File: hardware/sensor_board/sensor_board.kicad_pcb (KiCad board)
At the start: 2 copper layers, 18 x 15 mm, 4 parts, among them J0 Conn_01x04, U0 HIHxx3x-021

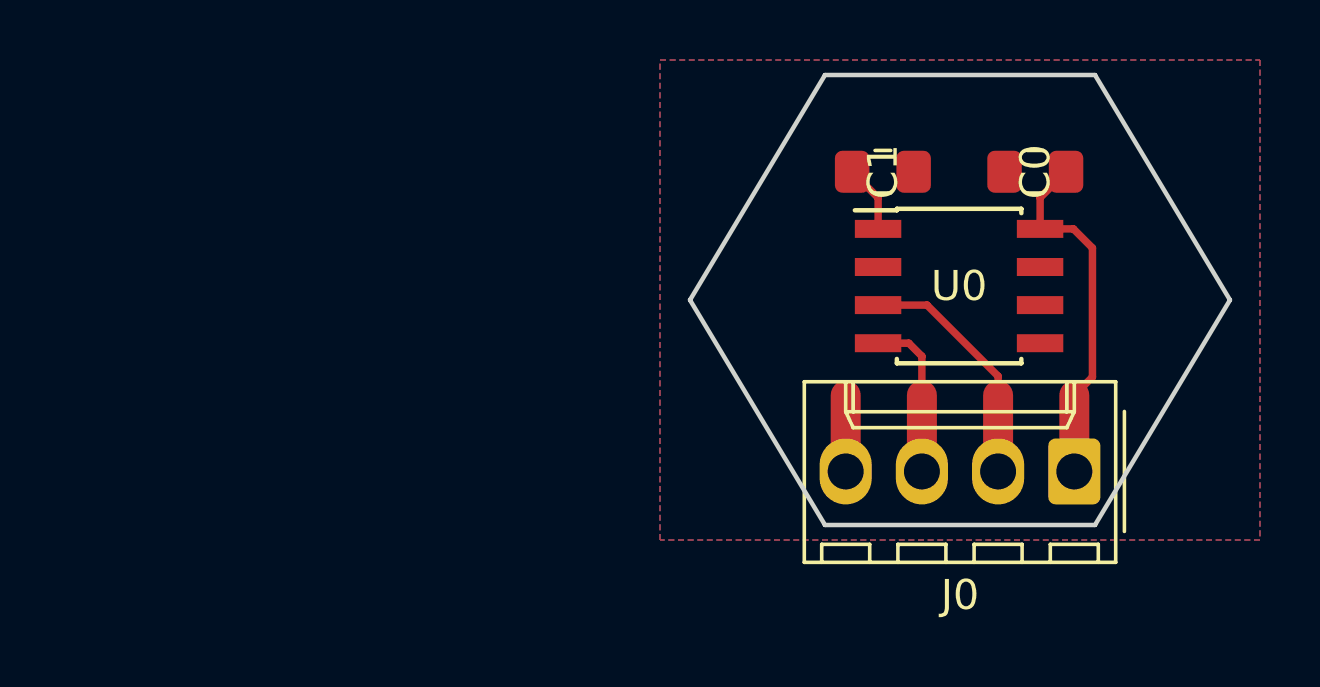
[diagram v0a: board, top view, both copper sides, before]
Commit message: Moving form multiplexer to two I2C busses
Changed from using one I2C bus with a multiplexer to using two I2C busses with the addition of level shifters
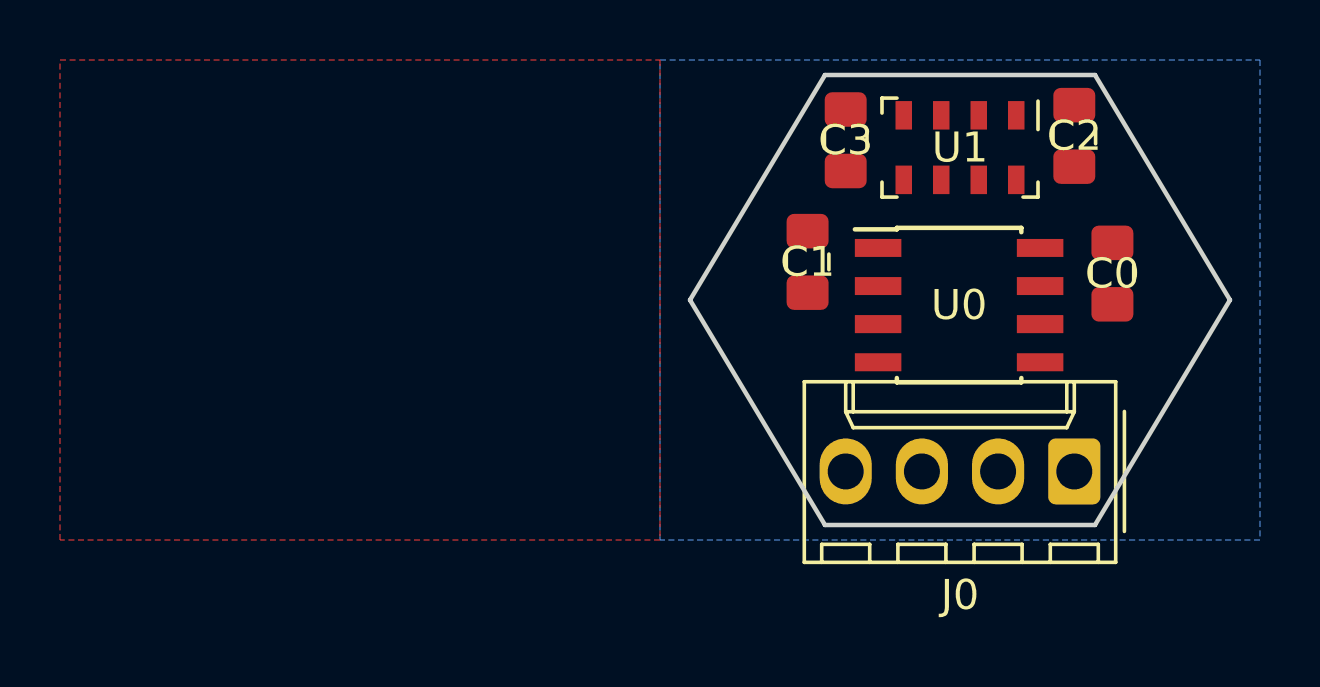
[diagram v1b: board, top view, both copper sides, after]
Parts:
- added C2: 1µ, Capacitor_SMD:C_0805_2012Metric_Pad1.15x1.40mm_HandSolder, F.Cu at (144.8, 84.5)
- added C3: 1µ, Capacitor_SMD:C_0805_2012Metric_Pad1.15x1.40mm_HandSolder, F.Cu at (137.2, 84.7)
- added U1: MPL115A2, Package_LGA:LGA-8_3x5mm_P1.25mm, F.Cu at (141.0, 84.9)
- moved C0 4.26 mm to (146.1, 89.1), turned to 90 degrees
- moved C1 3.92 mm to (135.9, 88.7), turned to 270 degrees
- moved U0 0.64 mm to (141.0, 90.2)
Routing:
- net +3V3: track 12.0 -> 0.00 mm
- net /SCL: track 8.16 -> 0.00 mm
- net /SDA: track 6.99 -> 0.16 mm
- net GND: track 2.54 -> 0.00 mm
- net /Vcore: track 2.26 -> 0.00 mm

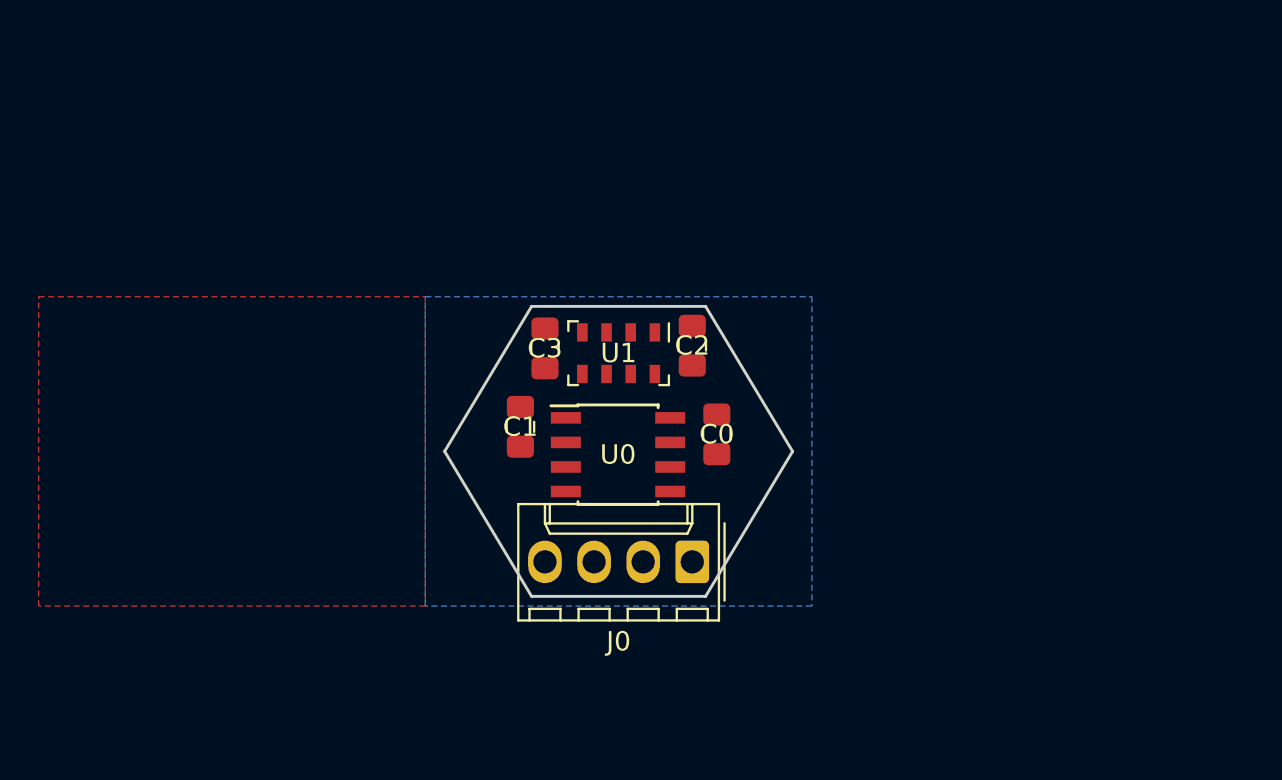
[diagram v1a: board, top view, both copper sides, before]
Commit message: Sensor board v2 and improvements to pHAT
Added a I2C level shifter to the sensor board, which lead to a complete redesign
Some graphical improvements to the pHAT
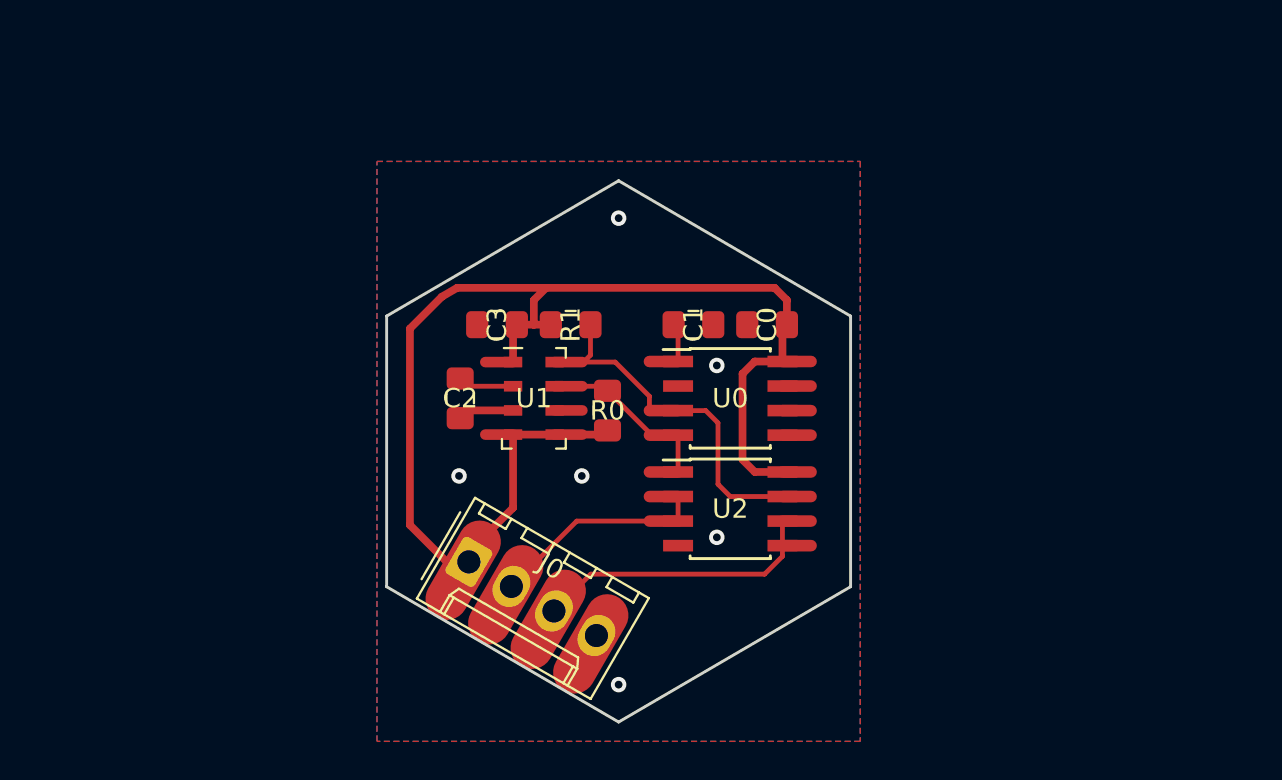
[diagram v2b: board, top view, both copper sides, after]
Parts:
- added R0: R, Resistor_SMD:R_0805_2012Metric_Pad1.15x1.40mm_HandSolder, F.Cu at (140.4, 87.9)
- added R1: R, Resistor_SMD:R_0805_2012Metric_Pad1.15x1.40mm_HandSolder, F.Cu at (138.5, 83.4)
- added U2: P82B96, Package_SO:SOIC-8_3.9x4.9mm_P1.27mm, F.Cu at (146.8, 93.0)
- moved C2 12.3 mm to (132.8, 87.3)
- moved J0 11.6 mm to (133.3, 95.7), turned to 330 degrees
- moved C1 10.4 mm to (144.9, 83.4), turned to 0 degrees
- moved U0 6.50 mm to (146.8, 87.3)
- moved C0 6.24 mm to (148.7, 83.4), turned to 180 degrees
- moved U1 4.97 mm to (136.6, 87.3), turned to 0 degrees
- moved C3 2.77 mm to (134.7, 83.4), turned to 180 degrees
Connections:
- J0 pad 2: /SCL -> /SCL_ext
- J0 pad 3: /SDA -> /SDA_ext
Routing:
- net +3V3: track 0.00 -> 74.6 mm
- net /SCL: track 0.00 -> 21.3 mm
- net /SDA_ext: track 0.00 -> 21.2 mm
- net /SCL_ext: track 0.00 -> 17.7 mm
- net /SDA: track 0.16 -> 12.8 mm
- net GND: track 0.00 -> 6.30 mm, vias 0 -> 6
- net /Vcore: track 0.00 -> 3.48 mm
- net Net-(C2-Pad1): track 0.00 -> 2.90 mm
- net Net-(U0-Pad7): track 0.00 -> 1.48 mm
- net Net-(U0-Pad6): track 0.00 -> 1.48 mm
- net Net-(U0-Pad5): track 0.00 -> 1.48 mm
- net Net-(U1-Pad6): track 0.00 -> 1.44 mm
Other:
- board size 18 x 15 mm -> 24 x 28 mm
- net class Power added: clearance 0.3, trace_width 0.4, via_dia 0.8, via_drill 0.4

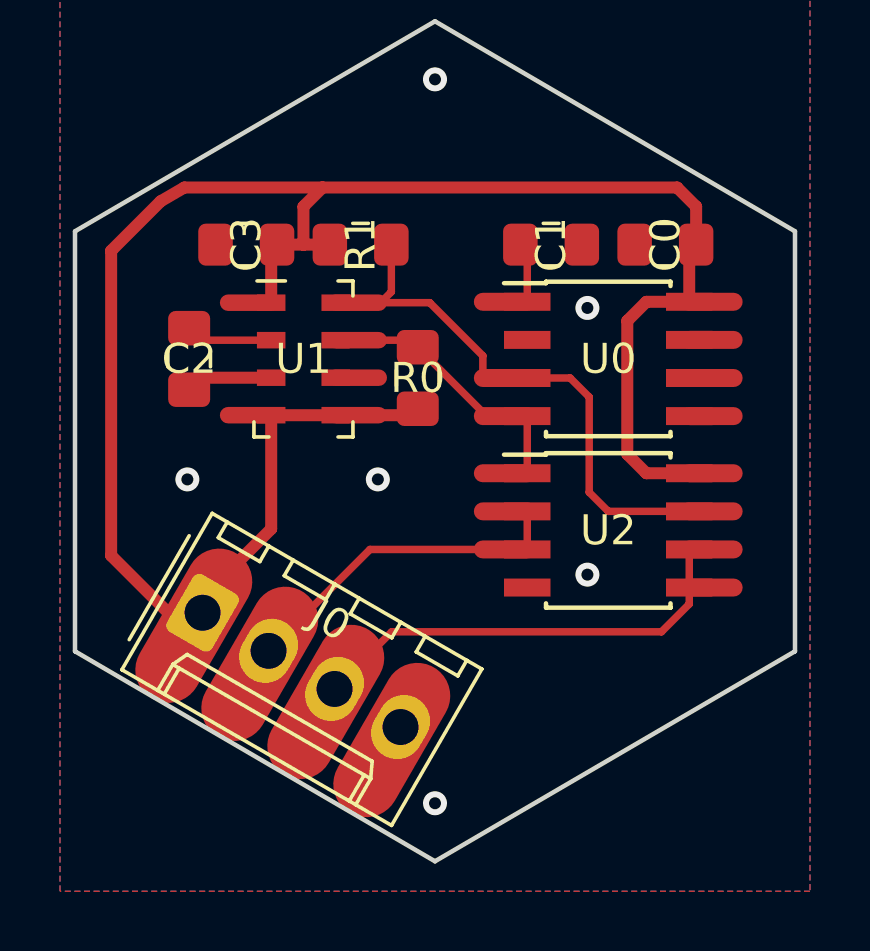
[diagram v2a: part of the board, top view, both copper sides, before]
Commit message: Added the alarm pin for humidity
Added support for the alarm pin of the HIH6131 in order to detect through interrupt a high level of humidity
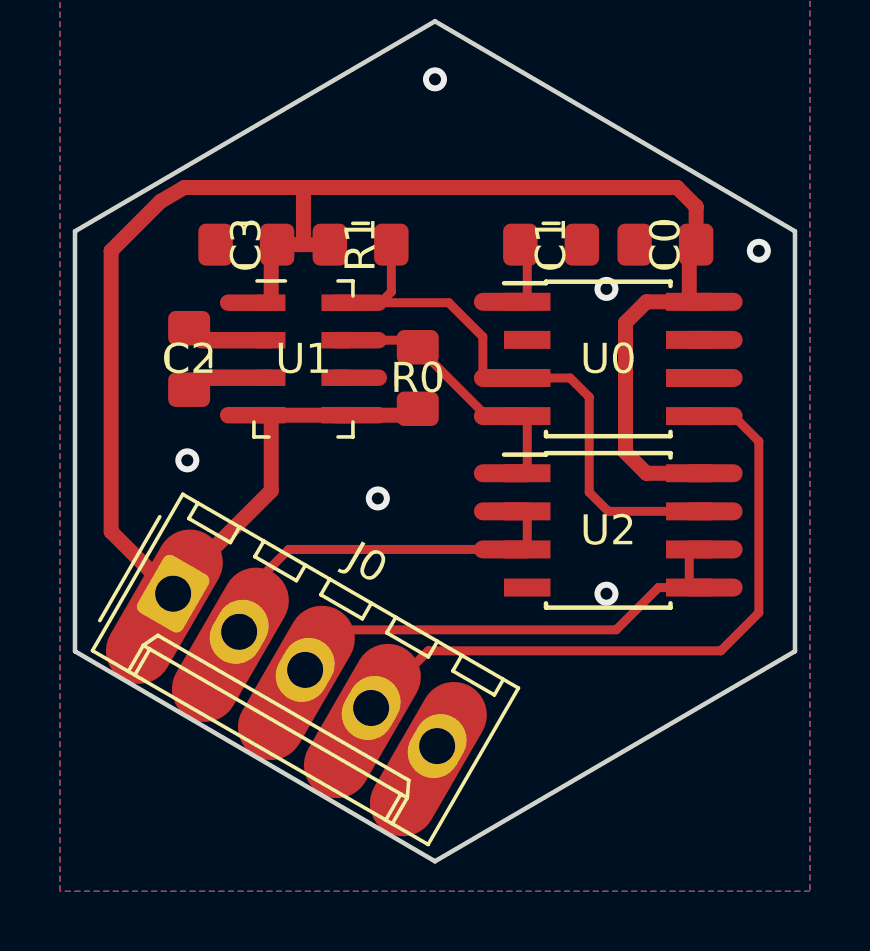
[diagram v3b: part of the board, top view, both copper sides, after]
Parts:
- J0: value Conn_01x04 -> Conn_01x05; footprint Connector_Molex:Molex_KK-254_AE-6410-04A_1x04_P2.54mm_Vertical -> Connector_Molex:Molex_KK-254_AE-6410-05A_1x05_P2.54mm_Vertical
- moved J0 1.17 mm to (132.3, 95.1)
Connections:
- J0 pad 4: GND -> /alarm
- U0 pad 5: Net-(U0-Pad5) -> /alarm
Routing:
- net /alarm: track 0.00 -> 26.0 mm
- net +3V3: track 74.6 -> 72.5 mm
- net Net-(U0-Pad5): track 1.48 -> 0.00 mm
- net /SCL_ext: track 17.7 -> 19.0 mm
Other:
- net class Default: trace_width 0.25 -> 0.3
- net class Power: trace_width 0.4 -> 0.5

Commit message: Start of hardware redesign
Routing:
- net GND: track 6.30 -> 2.90 mm
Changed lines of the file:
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@@
     (thickness 1.6)
     (drawings 7)
-    (tracks 97)
+    (tracks 96)
     (zones 0)
     (modules 10)
@@
   (gr_line (start 141 90) (end 134 102) (layer Dwgs.User) (width 0.2))
   (via (at 146.715 95.08) (size 0.8) (drill 0.4) (layers F.Cu B.Cu) (net 1))
-  (segment (start 139.928636 102.065) (end 141.628636 99.120514) (width 2.2) (layer F.Cu) (net 1))
   (segment (start 133.205 87.88) (end 132.805 88.28) (width 0.5) (layer F.Cu) (net 1))
   (segment (start 135.54 87.88) (end 133.205 87.88) (width 0.55) (layer F.Cu) (net 1))

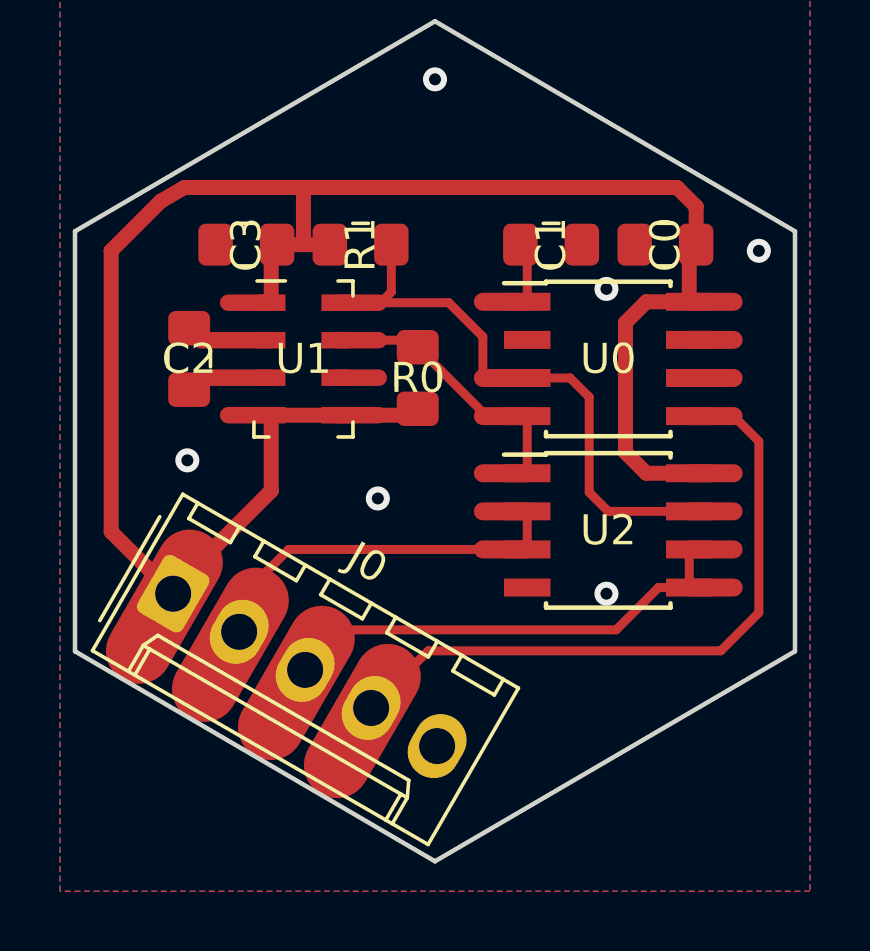
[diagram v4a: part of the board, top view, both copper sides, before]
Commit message: Preparing layout for adding a fan
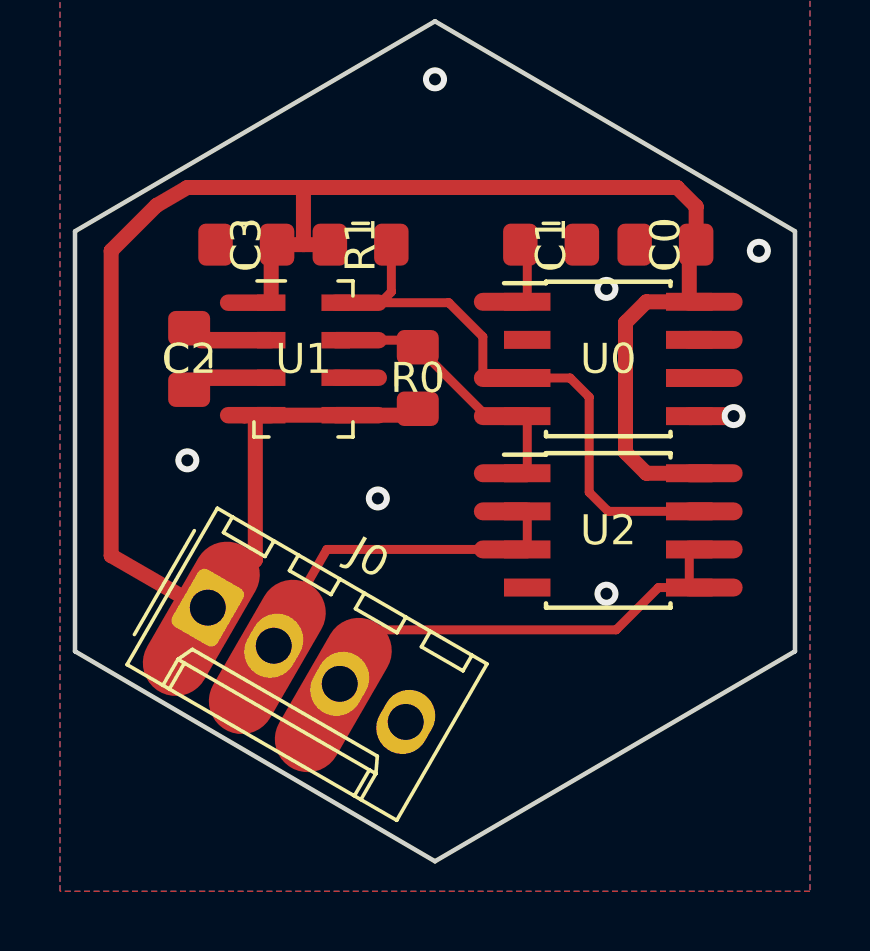
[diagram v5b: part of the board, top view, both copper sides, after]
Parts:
- J0: value Conn_01x05 -> Conn_01x04; footprint Connector_Molex:Molex_KK-254_AE-6410-05A_1x05_P2.54mm_Vertical -> Connector_Molex:Molex_KK-254_AE-6410-04A_1x04_P2.54mm_Vertical
- moved J0 1.24 mm to (133.4, 95.5)
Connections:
- J0 pad 4: /alarm -> GND
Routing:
- net /alarm: track 26.0 -> 1.48 mm, vias 0 -> 1
- net /SCL_ext: track 19.0 -> 14.7 mm
- net /SDA_ext: track 21.6 -> 19.7 mm
- net +3V3: track 72.5 -> 74.1 mm
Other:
- rule trace_min: 0.2 -> 0.3
